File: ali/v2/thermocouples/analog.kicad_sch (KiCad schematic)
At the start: 67 parts, among them J10 Conn_01x02, J11 Conn_01x02, J12 Conn_01x02, J13 Conn_01x02, J14 Conn_01x02, J9 Conn_01x02, U6 ADS124S08

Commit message: Small thermocouple notes: Considering changing biasing scheme
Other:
- note added: "Most likely going to convert this to use VBIAS and sacrifice two of the channels still yields better theoretical results than MAX31856 while being half the cost and more compact"
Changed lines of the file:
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@@
+		)
+	)
+	(text "Most likely going to convert this to use VBIAS and sacrifice two of the channels\nstill yields better theoretical results than MAX31856 while being half the cost\nand more compact"
+		(exclude_from_sim no)
+		(at 54.864 193.04 0)
+		(effects
+			(font
+				(size 1.27 1.27)
+			)
 		)
 	)

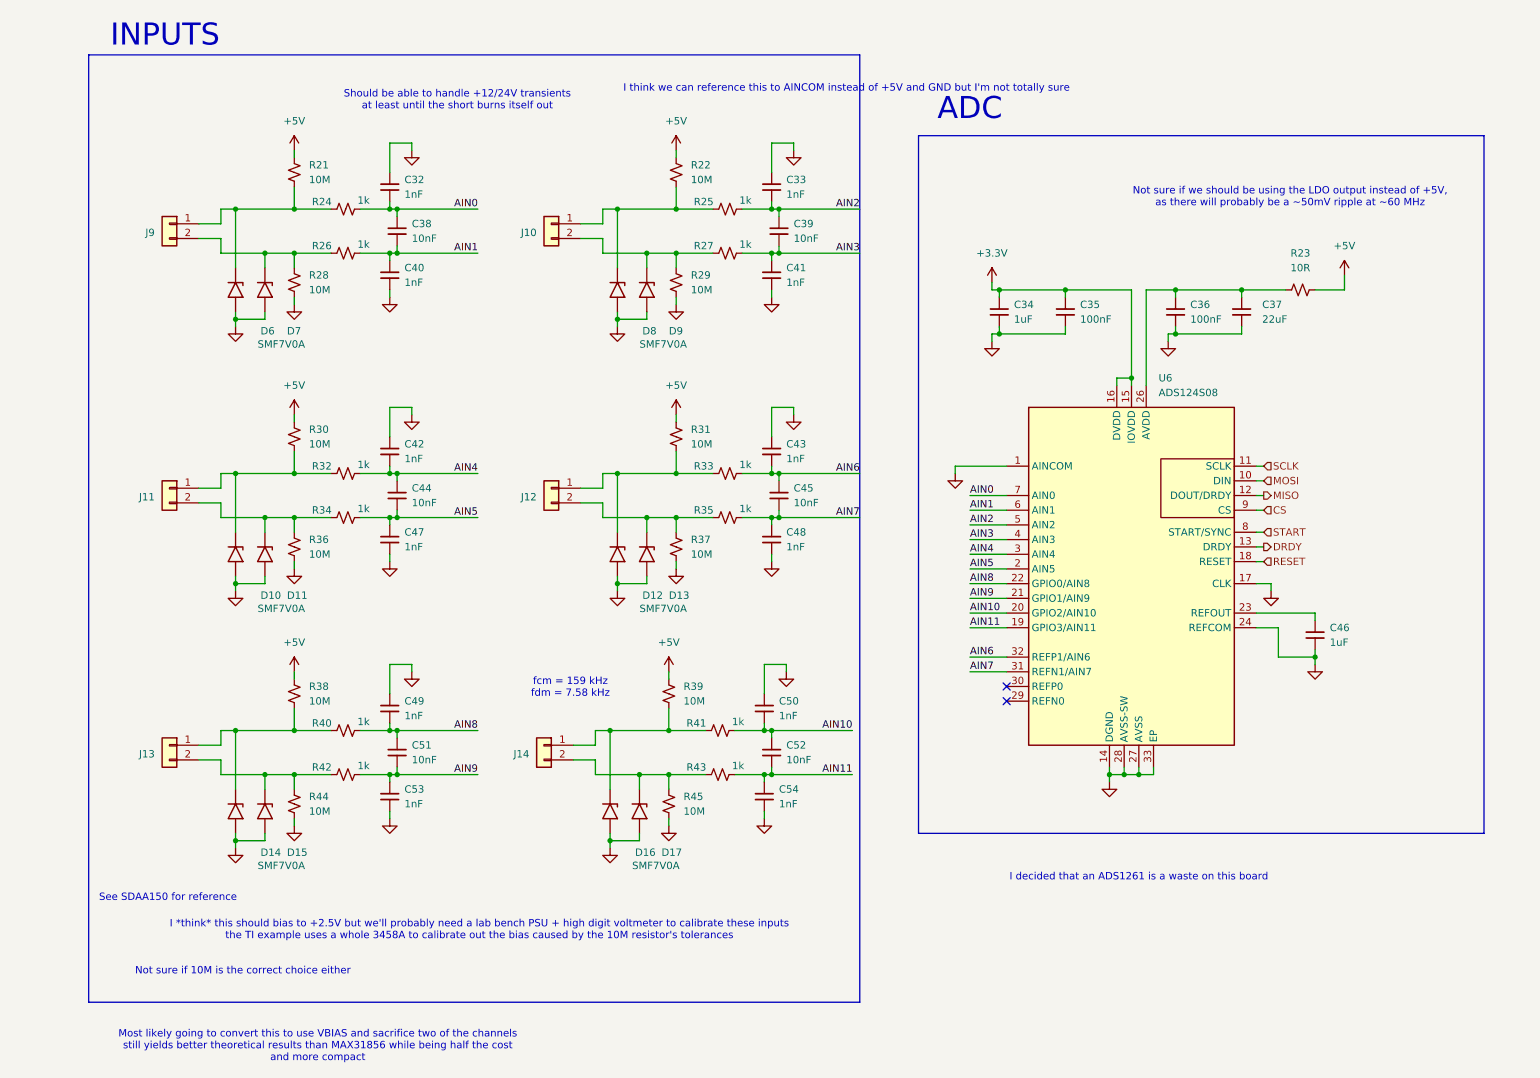
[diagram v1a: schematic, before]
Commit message: Document setup, update template, and use an ampersand when referring to APRL
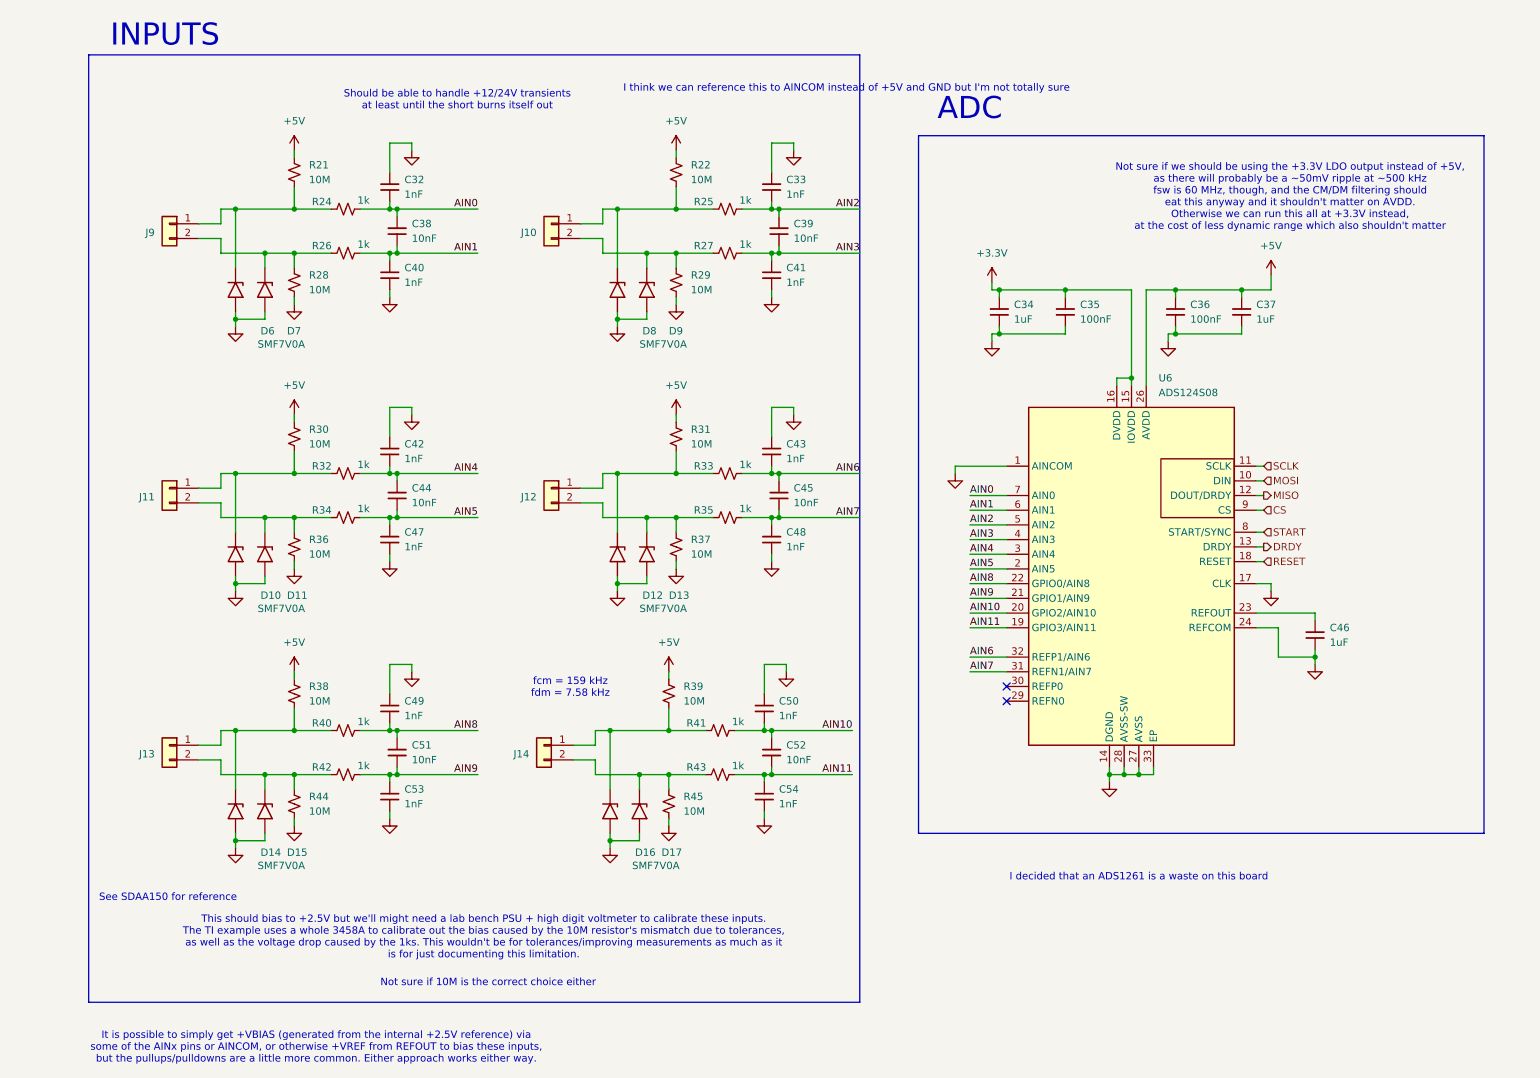
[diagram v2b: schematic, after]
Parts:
- removed R23: 10R, APRL_Passive:R_0603, symbol Device:R_Small_US
- C37: value 22uF -> 1uF; footprint APRL_Passive:C_0805 -> APRL_Passive:C_0603; MPN GRM21BZ71A226ME15 -> GRM188D72A105KE01
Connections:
- net +5V: now also C36.1, C37.1, U6.26 (AVDD)
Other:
- note added: "It is possible to simply get +VBIAS (generated from the internal +2.5V reference) via some of the AINx pins or AINCOM, or otherwise +VREF from REFOUT to bias these inputs, but the pullups/pulldowns are a little more common. Either approach works either way."
- note added: "Not sure if we should be using the +3.3V LDO output instead of +5V, as there will probably be a ~50mV ripple at ~500 kHz fsw is 60 MHz, though, and the CM/DM filtering should eat this anyway and it shouldn't matter on AVDD. Otherwise we can run this all at +3.3V instead, at the cost of less dynamic range which also shouldn't matter"
- note added: "This should bias to +2.5V but we'll might need a lab bench PSU + high digit voltmeter to calibrate these inputs. The TI example uses a whole 3458A to calibrate out the bias caused by the 10M resistor's mismatch due to tolerances, as well as the voltage drop caused by the 1ks. This wouldn't be for tolerances/improving measurements as much as it is for just documenting this limitation."
- note removed: "I *think* this should bias to +2.5V but we'll probably need a lab bench PSU + high digit voltmeter to calibrate these inputs the TI example uses a whole 3458A to calibrate out the bias caused by the 10M resistor's tolerances"
- note removed: "Most likely going to convert this to use VBIAS and sacrifice two of the channels still yields better theoretical results than MAX31856 while being half the cost and more compact"
- note removed: "Not sure if we should be using the LDO output instead of +5V, as there will probably be a ~50mV ripple at ~60 MHz"
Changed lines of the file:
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@@
 		)
 	)
-	(text "I *think* this should bias to +2.5V but we'll probably need a lab bench PSU + high digit voltmeter to calibrate these inputs\nthe TI example uses a whole 3458A to calibrate out the bias caused by the 10M resistor's tolerances"
+	(text "This should bias to +2.5V but we'll might need a lab bench PSU + high digit voltmeter to calibrate these inputs.\nThe TI example uses a whole 3458A to calibrate out the bias caused by the 10M resistor's mismatch due to tolerances,\nas well as the voltage drop caused by the 1ks. This wouldn't be for tolerances/improving measurements as much as it \nis for just documenting this limitation."
 		(exclude_from_sim no)
-		(at 82.804 172.974 0)
+		(at 83.566 174.244 0)
 		(effects
 			(font
@@
 	(text "Not sure if 10M is the correct choice either"
 		(exclude_from_sim no)
-		(at 41.91 180.086 0)
+		(at 84.328 182.118 0)
 		(effects
 			(font
@@
 		)
 	)
-	(text "Not sure if we should be using the LDO output instead of +5V,\nas there will probably be a ~50mV ripple at ~60 MHz"
+	(text "Not sure if we should be using the +3.3V LDO output instead of +5V,\nas there will probably be a ~50mV ripple at ~500 kHz\nfsw is 60 MHz, though, and the CM/DM filtering should\neat this anyway and it shouldn't matter on AVDD.\nOtherwise we can run this all at +3.3V instead,\nat the cost of less dynamic range which also shouldn't matter"
 		(exclude_from_sim no)
 		(at 223.012 46.228 0)
@@
 		)
 	)
-	(text "Most likely going to convert this to use VBIAS and sacrifice two of the channels\nstill yields better theoretical results than MAX31856 while being half the cost\nand more compact"
+	(text "It is possible to simply get +VBIAS (generated from the internal +2.5V reference) via\nsome of the AINx pins or AINCOM, or otherwise +VREF from REFOUT to bias these inputs,\nbut the pullups/pulldowns are a little more common. Either approach works either way."
 		(exclude_from_sim no)
-		(at 54.864 193.04 0)
+		(at 54.61 193.294 0)
 		(effects
 			(font
@@
 	(wire
 		(pts
-			(xy 227.33 62.23) (xy 232.41 62.23)
-		)
-		(stroke
-			(width 0)
-			(type default)
-		)
-	)
-	(wire
-		(pts
 			(xy 50.8 38.1) (xy 50.8 39.37)
 		)
@@
 	(wire
 		(pts
-			(xy 232.41 62.23) (xy 232.41 59.69)
+			(xy 219.71 62.23) (xy 219.71 59.69)
 		)
 		(stroke
@@
 	(wire
 		(pts
-			(xy 203.2 62.23) (xy 222.25 62.23)
+			(xy 203.2 62.23) (xy 219.71 62.23)
 		)
 		(stroke
@@
 	(symbol
 		(lib_id "power:+3.3V")
-		(at 232.41 59.69 0)
+		(at 219.71 59.69 0)
 		(unit 1)
 		(body_style 1)
@@
 		(fields_autoplaced yes)
 		(property "Reference" "#PWR065"
-			(at 232.41 63.5 0)
+			(at 219.71 63.5 0)
 			(hide yes)
 			(show_name no)
@@
 		)
 		(property "Value" "+5V"
-			(at 232.41 54.61 0)
+			(at 219.71 54.61 0)
 			(show_name no)
 			(do_not_autoplace no)
@@
 		)
 		(property "Footprint" ""
-			(at 232.41 59.69 0)
+			(at 219.71 59.69 0)
 			(hide yes)
 			(show_name no)
@@
 		)
 		(property "Datasheet" ""
-			(at 232.41 59.69 0)
+			(at 219.71 59.69 0)
 			(hide yes)
 			(show_name no)
@@
 		)
 		(property "Description" "Power symbol creates a global label with name \"+3.3V\""
-			(at 232.41 59.69 0)
+			(at 219.71 59.69 0)
 			(hide yes)
 			(show_name no)
@@
 	)
 	(symbol
-		(lib_id "Device:C_Small")
-		(at 214.63 66.04 0)
-		(unit 1)
-		(body_style 1)
-		(exclude_from_sim no)
-		(in_bom yes)
-		(on_board yes)
-		(in_pos_files yes)
-		(dnp no)
-		(property "Reference" "C37"
-			(at 218.186 64.77 0)
-			(show_name no)
-			(do_not_autoplace no)
-			(effects
-				(font
-					(size 1.27 1.27)
-				)
-				(justify left)
-			)
-		)
-		(property "Value" "22uF"
-			(at 218.186 67.31 0)
-			(show_name no)
-			(do_not_autoplace no)
-			(effects
-				(font
-					(size 1.27 1.27)
-				)
-				(justify left)
-			)
-		)
-		(property "Footprint" "APRL_Passive:C_0805"
-			(at 214.63 66.04 0)
-			(hide yes)
-			(show_name no)
-			(do_not_autoplace no)
-			(effects
-				(font
-					(size 1.27 1.27)
-				)
-			)
-		)
-		(property "Datasheet" ""
-			(at 214.63 66.04 0)
-			(hide yes)
-			(show_name no)
-			(do_not_autoplace no)
-			(effects
-				(font
-					(size 1.27 1.27)
-				)
-			)
-		)
-		(property "Description" "Unpolarized capacitor, small symbol"
-			(at 214.63 66.04 0)
-			(hide yes)
-			(show_name no)
-			(do_not_autoplace no)
-			(effects
-				(font
-					(size 1.27 1.27)
-				)
-			)
-		)
-		(property "MPN" "GRM21BZ71A226ME15"
-			(at 214.63 66.04 0)
-			(hide yes)
-			(show_name no)
-			(do_not_autoplace no)
-			(effects
-				(font
-					(size 1.27 1.27)
-				)
-			)
-		)
-		(property "MANUFACTURER" "Murata"
-			(at 214.63 66.04 0)
-			(hide yes)
-			(show_name no)
-			(do_not_autoplace no)
-			(effects
-				(font
-					(size 1.27 1.27)
-				)
-			)
-		)
-		(pin "2"
-		)
-		(pin "1"
-		)
-		(instances
-			(project "thermocouples"
-				(path "/0eb5ae8a-84ea-4b7e-bec4-bb4e0217d666/de3cef6c-f0bf-43f9-bc77-3e59044b84fe"
-					(reference "C37")
-					(unit 1)
-				)
-			)
-		)
-	)
-	(symbol
 		(lib_id "Connector_Generic:Conn_01x02")
 		(at 29.21 50.8 0)
@@
 	(symbol
 		(lib_id "Device:R_Small_US")
-		(at 224.79 62.23 90)
-		(unit 1)
-		(body_style 1)
-		(exclude_from_sim no)
-		(in_bom yes)
-		(on_board yes)
-		(in_pos_files yes)
-		(dnp no)
-		(fields_autoplaced yes)
-		(property "Reference" "R23"
-			(at 224.79 55.88 90)
-			(show_name no)
-			(do_not_autoplace no)
-			(effects
-				(font
-					(size 1.27 1.27)
-				)
-			)
-		)
-		(property "Value" "10R"
-			(at 224.79 58.42 90)
-			(show_name no)
-			(do_not_autoplace no)
-			(effects
-				(font
-					(size 1.27 1.27)
-				)
-			)
-		)
-		(property "Footprint" "APRL_Passive:R_0603"
-			(at 224.79 62.23 0)
-			(hide yes)
-			(show_name no)
-			(do_not_autoplace no)
-			(effects
-				(font
-					(size 1.27 1.27)
-				)
-			)
-		)
-		(property "Datasheet" ""
-			(at 224.79 62.23 0)
-			(hide yes)
-			(show_name no)
-			(do_not_autoplace no)
-			(effects
-				(font
-					(size 1.27 1.27)
-				)
-			)
-		)
-		(property "Description" "Resistor, small US symbol"
-			(at 224.79 62.23 0)
-			(hide yes)
-			(show_name no)
-			(do_not_autoplace no)
-			(effects
-				(font
-					(size 1.27 1.27)
-				)
-			)
-		)
-		(property "MPN" "RC0603FR-0710RL"
-			(at 224.79 62.23 90)
-			(hide yes)
-			(show_name no)
-			(do_not_autoplace no)
-			(effects
-				(font
-					(size 1.27 1.27)
-				)
-			)
-		)
-		(property "MANUFACTURER" "Yageo"
-			(at 224.79 62.23 90)
-			(hide yes)
-			(show_name no)
-			(do_not_autoplace no)
-			(effects
-				(font
-					(size 1.27 1.27)
-				)
-			)
-		)
-		(pin "1"
-		)
-		(pin "2"
-		)
-		(instances
-			(project "thermocouples"
-				(path "/0eb5ae8a-84ea-4b7e-bec4-bb4e0217d666/de3cef6c-f0bf-43f9-bc77-3e59044b84fe"
-					(reference "R23")
-					(unit 1)
-				)
-			)
-		)
-	)
-	(symbol
-		(lib_id "Device:R_Small_US")
 		(at 116.84 106.68 0)
 		(unit 1)
@@
 					(unit 1)
 				)
+			)
+		)
+	)
+	(symbol
+		(lib_id "Device:C_Small")
+		(at 214.63 66.04 0)
+		(unit 1)
+		(body_style 1)
+		(exclude_from_sim no)
+		(in_bom yes)
+		(on_board yes)
+		(in_pos_files yes)
+		(dnp no)
+		(fields_autoplaced yes)
+		(property "Reference" "C37"
+			(at 217.17 64.7762 0)
+			(show_name no)
+			(do_not_autoplace no)
+			(effects
+				(font
+					(size 1.27 1.27)
+				)
+				(justify left)
+			)
+		)
+		(property "Value" "1uF"
+			(at 217.17 67.3162 0)
+			(show_name no)
+			(do_not_autoplace no)
+			(effects
+				(font
+					(size 1.27 1.27)
+				)
+				(justify left)
+			)
+		)
+		(property "Footprint" "APRL_Passive:C_0603"
+			(at 214.63 66.04 0)
+			(hide yes)
+			(show_name no)
+			(do_not_autoplace no)
+			(effects
+				(font
+					(size 1.27 1.27)
+				)
+			)
+		)
+		(property "Datasheet" ""
+			(at 214.63 66.04 0)
+			(hide yes)
+			(show_name no)
+			(do_not_autoplace no)
+			(effects
+				(font
+					(size 1.27 1.27)
+				)
+			)
+		)
+		(property "Description" "Unpolarized capacitor, small symbol"
+			(at 214.63 66.04 0)
+			(hide yes)
+			(show_name no)
+			(do_not_autoplace no)
+			(effects
+				(font
+					(size 1.27 1.27)
+				)
+			)
+		)
+		(property "MPN" "GRM188D72A105KE01"
+			(at 214.63 66.04 0)
+			(hide yes)
+			(show_name no)
+			(do_not_autoplace no)
+			(effects
+				(font
+					(size 1.27 1.27)
+				)
+			)
+		)
+		(property "MANUFACTURER" "Murata"
+			(at 214.63 66.04 0)
+			(hide yes)
+			(show_name no)
+			(do_not_autoplace no)
+			(effects
+				(font
+					(size 1.27 1.27)
+				)
+			)
+		)
+		(pin "2"
+		)
+		(pin "1"
+		)
+		(instances
+			(project "thermocouples"
+				(path "/0eb5ae8a-84ea-4b7e-bec4-bb4e0217d666/de3cef6c-f0bf-43f9-bc77-3e59044b84fe"
+					(reference "C37")
+					(unit 1)
+				)

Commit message: Begin prep for second board review
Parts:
- removed R21, R22, R38, R39, R44, R45: 10M, APRL_Passive:R_0603, symbol Device:R_Small_US
- D10, D11, D12, D13, D14, D15, D16, D17, D6, D7, D8, D9: value SMF7V0A -> VTVS28ASMF; MPN SMF7V0A-E3-18 -> VTVS28ASMF-M3-08
- R24, R25, R26, R27, R32, R33, R34, R35, R40, R41, R42, R43: value 1k -> 4.7k; MPN RT0603BRD071KL -> RT0603BRD074K7L
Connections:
- net +5V: no longer R30.1, R31.1
- net GND: no longer R28.2, R29.2, R36.2, R37.2
- net at D10.1 (A1), J11.1 (Pin_1), R32.1: no longer R30.2
- net at D9.1 (A1), J10.2 (Pin_2), R27.1: now also R30.2; no longer R29.1
- net at D15.1 (A1), J13.2 (Pin_2), R42.1: now also R36.2
- net at D13.1 (A1), J12.2 (Pin_2), R35.1: now also R31.2; no longer R37.1
- net at D17.1 (A1), J14.2 (Pin_2), R43.1: now also R37.2
- net at D12.1 (A1), J12.1 (Pin_1), R33.1: no longer R31.2
- net +ADC_VREF: now reaches C46.1, U6.23 (REFOUT)
- net +ADC_VREF: now also R28.1, R29.1, R30.1, R31.1, R36.1, R37.1
- net at D7.1 (A1), J9.2 (Pin_2), R26.1: now also R28.2; no longer R28.1
- net at D11.1 (A1), J11.2 (Pin_2), R34.1: now also R29.2; no longer R36.1
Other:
- note added: "fcm = 33.9 kHz fdm = 1.61 kHz"
- note removed: "I decided that an ADS1261 is a waste on this board"
- note removed: "I think we can reference this to AINCOM instead of +5V and GND but I'm not totally sure"
- note removed: "It is possible to simply get +VBIAS (generated from the internal +2.5V reference) via some of the AINx pins or AINCOM, or otherwise +VREF from REFOUT to bias these inputs, but the pullups/pulldowns are a little more common. Either approach works either way."
- note removed: "Not sure if 10M is the correct choice either"
- note removed: "Not sure if we should be using the +3.3V LDO output instead of +5V, as there will probably be a ~50mV ripple at ~500 kHz fsw is 60 MHz, though, and the CM/DM filtering should eat this anyway and it shouldn't matter on AVDD. Otherwise we can run this all at +3.3V instead, at the cost of less dynamic range which also shouldn't matter"
- note removed: "This should bias to +2.5V but we'll might need a lab bench PSU + high digit voltmeter to calibrate these inputs. The TI example uses a whole 3458A to calibrate out the bias caused by the 10M resistor's mismatch due to tolerances, as well as the voltage drop caused by the 1ks. This wouldn't be for tolerances/improving measurements as much as it is for just documenting this limitation."
- note removed: "fcm = 159 kHz fdm = 7.58 kHz"
- moved on the sheet: C32, C33, C38, C39, C40, C41, C42, C43, C44, C45, C47, C48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
